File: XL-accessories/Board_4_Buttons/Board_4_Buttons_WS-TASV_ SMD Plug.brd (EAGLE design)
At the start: 156 x 47.9 mm, 5 parts, among them J2 691709710305

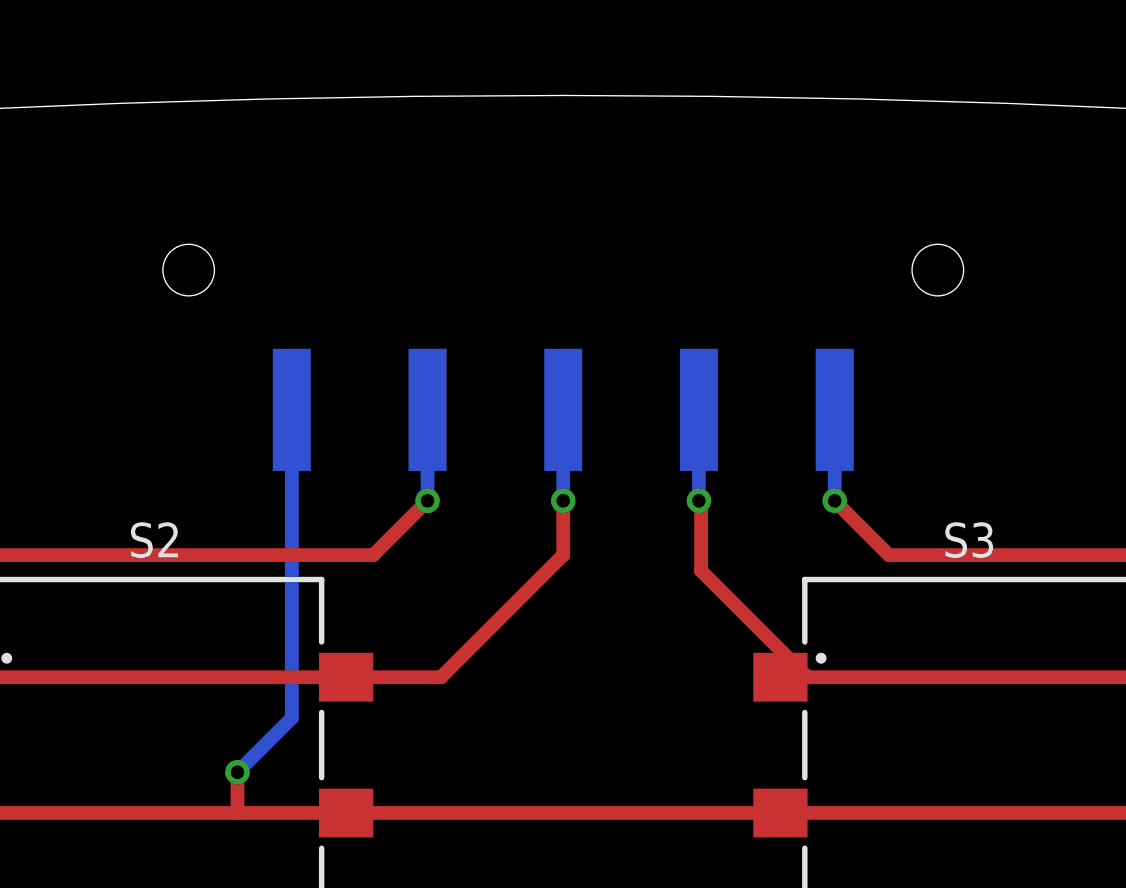
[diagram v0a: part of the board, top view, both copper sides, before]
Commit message: Update connector element position and wire coordinates in board design file
The commit updates the position of a connector element and adjusts wire coordinates in the board design file.
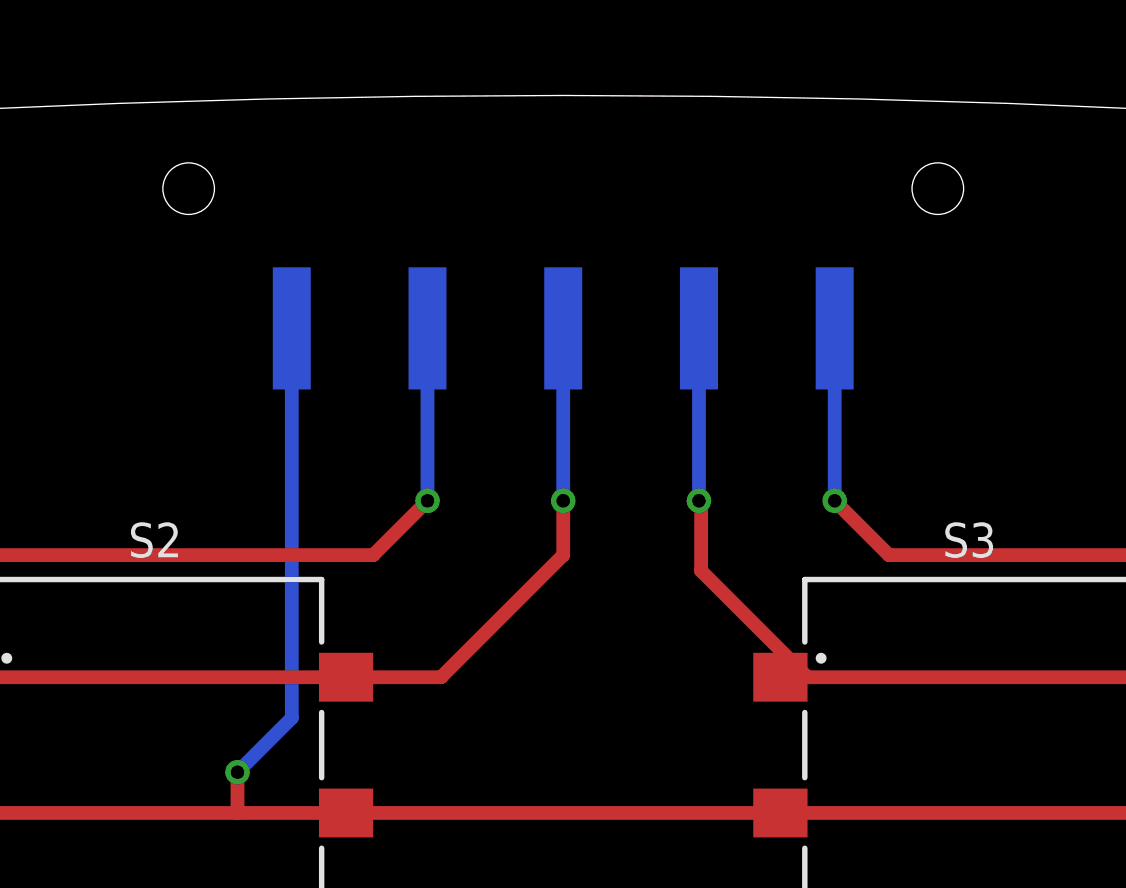
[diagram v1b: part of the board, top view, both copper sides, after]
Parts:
- moved J2 3.00 mm to (0.00, 20.5)
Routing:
- net N$8: track 48.3 -> 51.3 mm
- net N$7: track 25.5 -> 28.5 mm
- net N$6: track 29.2 -> 32.2 mm
- net N$5: track 54.0 -> 57.0 mm
- net N$1: track 119.7 -> 122.7 mm
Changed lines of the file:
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@@
 <attribute name="VALUE" value="430162073826" x="41.506" y="-7.8258" size="1.27" layer="27"/>
 </element>
-<element name="J2" library="Wurth_Connectors_WR-TBL Rising Cage Clamp" library_urn="urn:adsk.eagle:library:16280519" package="691709710305" package3d_urn="urn:adsk.eagle:package:16248446/4" value="691709710305" x="0" y="17.5" smashed="yes" rot="MR180">
-<attribute name="DATASHEET-URL" value="https://www.we-online.com/redexpert/spec/691709710305?ae" x="0" y="17.5" size="1.778" layer="28" rot="MR180" display="off"/>
-<attribute name="IR-UL" value="6A" x="0" y="17.5" size="1.778" layer="28" rot="MR180" display="off"/>
-<attribute name="MOUNT" value="THT" x="0" y="17.5" size="1.778" layer="28" rot="MR180" display="off"/>
-<attribute name="NAME" x="0" y="9" size="1.27" layer="26" rot="MR180" align="bottom-center"/>
-<attribute name="PART-NUMBER" value=" 691709710305 " x="0" y="17.5" size="1.778" layer="28" rot="MR180" display="off"/>
-<attribute name="PINS" value=" 5 " x="0" y="17.5" size="1.778" layer="28" rot="MR180" display="off"/>
-<attribute name="PITCH" value="5mm" x="0" y="17.5" size="1.778" layer="28" rot="MR180" display="off"/>
-<attribute name="TYPE" value="Horizontal" x="0" y="17.5" size="1.778" layer="28" rot="MR180" display="off"/>
-<attribute name="VALUE" x="0" y="23.5" size="1.27" layer="28" rot="MR180" align="bottom-center"/>
-<attribute name="WIRE" value="33 to 14 (AWG) 0.2 to 1.5 (mm²)" x="0" y="17.5" size="1.778" layer="28" rot="MR180" display="off"/>
-<attribute name="WORKING-VOLTAGE-UL" value="300V (AC)" x="0" y="17.5" size="1.778" layer="28" rot="MR180" display="off"/>
+<element name="J2" library="Wurth_Connectors_WR-TBL Rising Cage Clamp" library_urn="urn:adsk.eagle:library:16280519" package="691709710305" package3d_urn="urn:adsk.eagle:package:16248446/4" value="691709710305" x="0" y="20.5" smashed="yes" rot="MR180">
+<attribute name="DATASHEET-URL" value="https://www.we-online.com/redexpert/spec/691709710305?ae" x="0" y="20.5" size="1.778" layer="28" rot="MR180" display="off"/>
+<attribute name="IR-UL" value="6A" x="0" y="20.5" size="1.778" layer="28" rot="MR180" display="off"/>
+<attribute name="MOUNT" value="THT" x="0" y="20.5" size="1.778" layer="28" rot="MR180" display="off"/>
+<attribute name="NAME" x="0" y="12" size="1.27" layer="26" rot="MR180" align="bottom-center"/>
+<attribute name="PART-NUMBER" value=" 691709710305 " x="0" y="20.5" size="1.778" layer="28" rot="MR180" display="off"/>
+<attribute name="PINS" value=" 5 " x="0" y="20.5" size="1.778" layer="28" rot="MR180" display="off"/>
+<attribute name="PITCH" value="5mm" x="0" y="20.5" size="1.778" layer="28" rot="MR180" display="off"/>
+<attribute name="TYPE" value="Horizontal" x="0" y="20.5" size="1.778" layer="28" rot="MR180" display="off"/>
+<attribute name="VALUE" x="0" y="26.5" size="1.27" layer="28" rot="MR180" align="bottom-center"/>
+<attribute name="WIRE" value="33 to 14 (AWG) 0.2 to 1.5 (mm²)" x="0" y="20.5" size="1.778" layer="28" rot="MR180" display="off"/>
+<attribute name="WORKING-VOLTAGE-UL" value="300V (AC)" x="0" y="20.5" size="1.778" layer="28" rot="MR180" display="off"/>
 </element>
 </elements>
@@
 <contactref element="J2" pad="1"/>
 <wire x1="-10" y1="1" x2="-12" y2="-1" width="0.508" layer="16"/>
-<wire x1="-10" y1="12.35" x2="-10" y2="1" width="0.508" layer="16"/>
+<wire x1="-10" y1="15.35" x2="-10" y2="1" width="0.508" layer="16"/>
 </signal>
 <signal name="N$5">
@@
 <wire x1="-39" y1="2.5" x2="-34.5" y2="7" width="0.508" layer="1"/>
 <contactref element="J2" pad="2"/>
-<wire x1="-5" y1="12.35" x2="-5" y2="9" width="0.508" layer="16"/>
+<wire x1="-5" y1="15.35" x2="-5" y2="9" width="0.508" layer="16"/>
 <via x="-5" y="9" extent="1-16" drill="0.5"/>
 <wire x1="-7" y1="7" x2="-5" y2="9" width="0.508" layer="1"/>
@@
 <wire x1="-4.5" y1="2.5" x2="0" y2="7" width="0.508" layer="1"/>
 <contactref element="J2" pad="3"/>
-<wire x1="0" y1="12.35" x2="0" y2="9" width="0.508" layer="16"/>
+<wire x1="0" y1="15.35" x2="0" y2="9" width="0.508" layer="16"/>
 <via x="0" y="9" extent="1-16" drill="0.5"/>
 <wire x1="0" y1="7" x2="0" y2="9" width="0.508" layer="1"/>
@@
 <wire x1="5.08" y1="6.42" x2="9" y2="2.5" width="0.508" layer="1"/>
 <contactref element="J2" pad="4"/>
-<wire x1="5" y1="12.35" x2="5" y2="9" width="0.508" layer="16"/>
+<wire x1="5" y1="15.35" x2="5" y2="9" width="0.508" layer="16"/>
 <via x="5" y="9" extent="1-16" drill="0.5"/>
 <wire x1="5" y1="9" x2="5.08" y2="8.92" width="0.508" layer="1"/>
@@
 <wire x1="38" y1="2.5" x2="34.25" y2="7" width="0.508" layer="1"/>
 <contactref element="J2" pad="5"/>
-<wire x1="10" y1="12.35" x2="10" y2="9" width="0.508" layer="16"/>
+<wire x1="10" y1="15.35" x2="10" y2="9" width="0.508" layer="16"/>
 <via x="10" y="9" extent="1-16" drill="0.5"/>
 <wire x1="12" y1="7" x2="10" y2="9" width="0.508" layer="1"/>

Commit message: Update connector element position and attributes in the board design file.
- Adjusted the position and attributes of connector element J2 on the board.
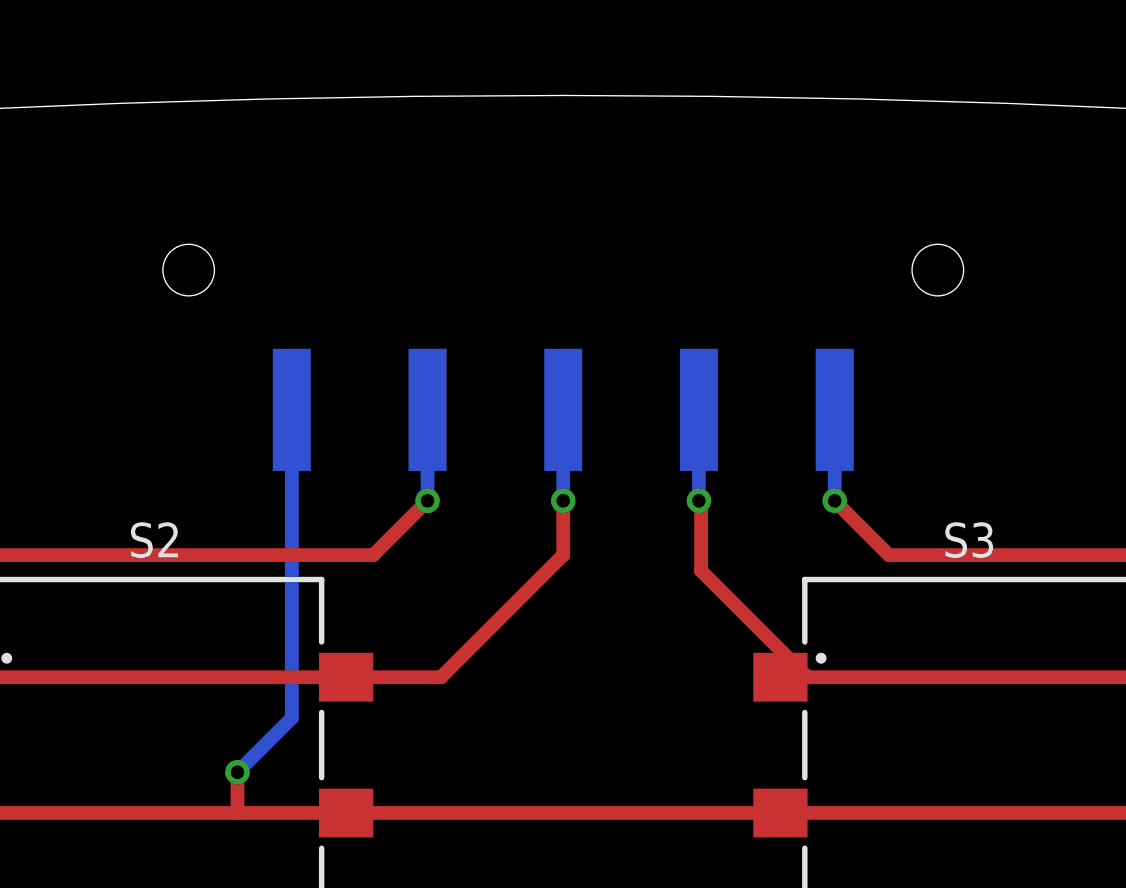
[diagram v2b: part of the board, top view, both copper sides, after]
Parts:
- moved J2 3.00 mm to (0.00, 17.5)
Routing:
- net N$8: track 51.3 -> 48.3 mm
- net N$7: track 28.5 -> 25.5 mm
- net N$6: track 32.2 -> 29.2 mm
- net N$5: track 57.0 -> 54.0 mm
- net N$1: track 122.7 -> 119.7 mm
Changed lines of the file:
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@@
 <attribute name="VALUE" value="430162073826" x="41.506" y="-7.8258" size="1.27" layer="27"/>
 </element>
-<element name="J2" library="Wurth_Connectors_WR-TBL Rising Cage Clamp" library_urn="urn:adsk.eagle:library:16280519" package="691709710305" package3d_urn="urn:adsk.eagle:package:16248446/4" value="691709710305" x="0" y="20.5" smashed="yes" rot="MR180">
-<attribute name="DATASHEET-URL" value="https://www.we-online.com/redexpert/spec/691709710305?ae" x="0" y="20.5" size="1.778" layer="28" rot="MR180" display="off"/>
-<attribute name="IR-UL" value="6A" x="0" y="20.5" size="1.778" layer="28" rot="MR180" display="off"/>
-<attribute name="MOUNT" value="THT" x="0" y="20.5" size="1.778" layer="28" rot="MR180" display="off"/>
-<attribute name="NAME" x="0" y="12" size="1.27" layer="26" rot="MR180" align="bottom-center"/>
-<attribute name="PART-NUMBER" value=" 691709710305 " x="0" y="20.5" size="1.778" layer="28" rot="MR180" display="off"/>
-<attribute name="PINS" value=" 5 " x="0" y="20.5" size="1.778" layer="28" rot="MR180" display="off"/>
-<attribute name="PITCH" value="5mm" x="0" y="20.5" size="1.778" layer="28" rot="MR180" display="off"/>
-<attribute name="TYPE" value="Horizontal" x="0" y="20.5" size="1.778" layer="28" rot="MR180" display="off"/>
-<attribute name="VALUE" x="0" y="26.5" size="1.27" layer="28" rot="MR180" align="bottom-center"/>
-<attribute name="WIRE" value="33 to 14 (AWG) 0.2 to 1.5 (mm²)" x="0" y="20.5" size="1.778" layer="28" rot="MR180" display="off"/>
-<attribute name="WORKING-VOLTAGE-UL" value="300V (AC)" x="0" y="20.5" size="1.778" layer="28" rot="MR180" display="off"/>
+<element name="J2" library="Wurth_Connectors_WR-TBL Rising Cage Clamp" library_urn="urn:adsk.eagle:library:16280519" package="691709710305" package3d_urn="urn:adsk.eagle:package:16248446/4" value="691709710305" x="0" y="17.5" smashed="yes" rot="MR180">
+<attribute name="DATASHEET-URL" value="https://www.we-online.com/redexpert/spec/691709710305?ae" x="0" y="17.5" size="1.778" layer="28" rot="MR180" display="off"/>
+<attribute name="IR-UL" value="6A" x="0" y="17.5" size="1.778" layer="28" rot="MR180" display="off"/>
+<attribute name="MOUNT" value="THT" x="0" y="17.5" size="1.778" layer="28" rot="MR180" display="off"/>
+<attribute name="NAME" x="0" y="9" size="1.27" layer="26" rot="MR180" align="bottom-center"/>
+<attribute name="PART-NUMBER" value=" 691709710305 " x="0" y="17.5" size="1.778" layer="28" rot="MR180" display="off"/>
+<attribute name="PINS" value=" 5 " x="0" y="17.5" size="1.778" layer="28" rot="MR180" display="off"/>
+<attribute name="PITCH" value="5mm" x="0" y="17.5" size="1.778" layer="28" rot="MR180" display="off"/>
+<attribute name="TYPE" value="Horizontal" x="0" y="17.5" size="1.778" layer="28" rot="MR180" display="off"/>
+<attribute name="VALUE" x="0" y="23.5" size="1.27" layer="28" rot="MR180" align="bottom-center"/>
+<attribute name="WIRE" value="33 to 14 (AWG) 0.2 to 1.5 (mm²)" x="0" y="17.5" size="1.778" layer="28" rot="MR180" display="off"/>
+<attribute name="WORKING-VOLTAGE-UL" value="300V (AC)" x="0" y="17.5" size="1.778" layer="28" rot="MR180" display="off"/>
 </element>
 </elements>
@@
 <contactref element="J2" pad="1"/>
 <wire x1="-10" y1="1" x2="-12" y2="-1" width="0.508" layer="16"/>
-<wire x1="-10" y1="15.35" x2="-10" y2="1" width="0.508" layer="16"/>
+<wire x1="-10" y1="12.35" x2="-10" y2="1" width="0.508" layer="16"/>
 </signal>
 <signal name="N$5">
@@
 <wire x1="-39" y1="2.5" x2="-34.5" y2="7" width="0.508" layer="1"/>
 <contactref element="J2" pad="2"/>
-<wire x1="-5" y1="15.35" x2="-5" y2="9" width="0.508" layer="16"/>
+<wire x1="-5" y1="12.35" x2="-5" y2="9" width="0.508" layer="16"/>
 <via x="-5" y="9" extent="1-16" drill="0.5"/>
 <wire x1="-7" y1="7" x2="-5" y2="9" width="0.508" layer="1"/>
@@
 <wire x1="-4.5" y1="2.5" x2="0" y2="7" width="0.508" layer="1"/>
 <contactref element="J2" pad="3"/>
-<wire x1="0" y1="15.35" x2="0" y2="9" width="0.508" layer="16"/>
+<wire x1="0" y1="12.35" x2="0" y2="9" width="0.508" layer="16"/>
 <via x="0" y="9" extent="1-16" drill="0.5"/>
 <wire x1="0" y1="7" x2="0" y2="9" width="0.508" layer="1"/>
@@
 <wire x1="5.08" y1="6.42" x2="9" y2="2.5" width="0.508" layer="1"/>
 <contactref element="J2" pad="4"/>
-<wire x1="5" y1="15.35" x2="5" y2="9" width="0.508" layer="16"/>
+<wire x1="5" y1="12.35" x2="5" y2="9" width="0.508" layer="16"/>
 <via x="5" y="9" extent="1-16" drill="0.5"/>
 <wire x1="5" y1="9" x2="5.08" y2="8.92" width="0.508" layer="1"/>
@@
 <wire x1="38" y1="2.5" x2="34.25" y2="7" width="0.508" layer="1"/>
 <contactref element="J2" pad="5"/>
-<wire x1="10" y1="15.35" x2="10" y2="9" width="0.508" layer="16"/>
+<wire x1="10" y1="12.35" x2="10" y2="9" width="0.508" layer="16"/>
 <via x="10" y="9" extent="1-16" drill="0.5"/>
 <wire x1="12" y1="7" x2="10" y2="9" width="0.508" layer="1"/>
